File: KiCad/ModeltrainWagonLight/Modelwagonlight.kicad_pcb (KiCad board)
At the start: 2 copper layers, 19.3 x 10.2 mm, 13 parts, among them J1 Conn_01x02, J2 Conn_01x02, U1 NCP1117-ADJ_SOT223

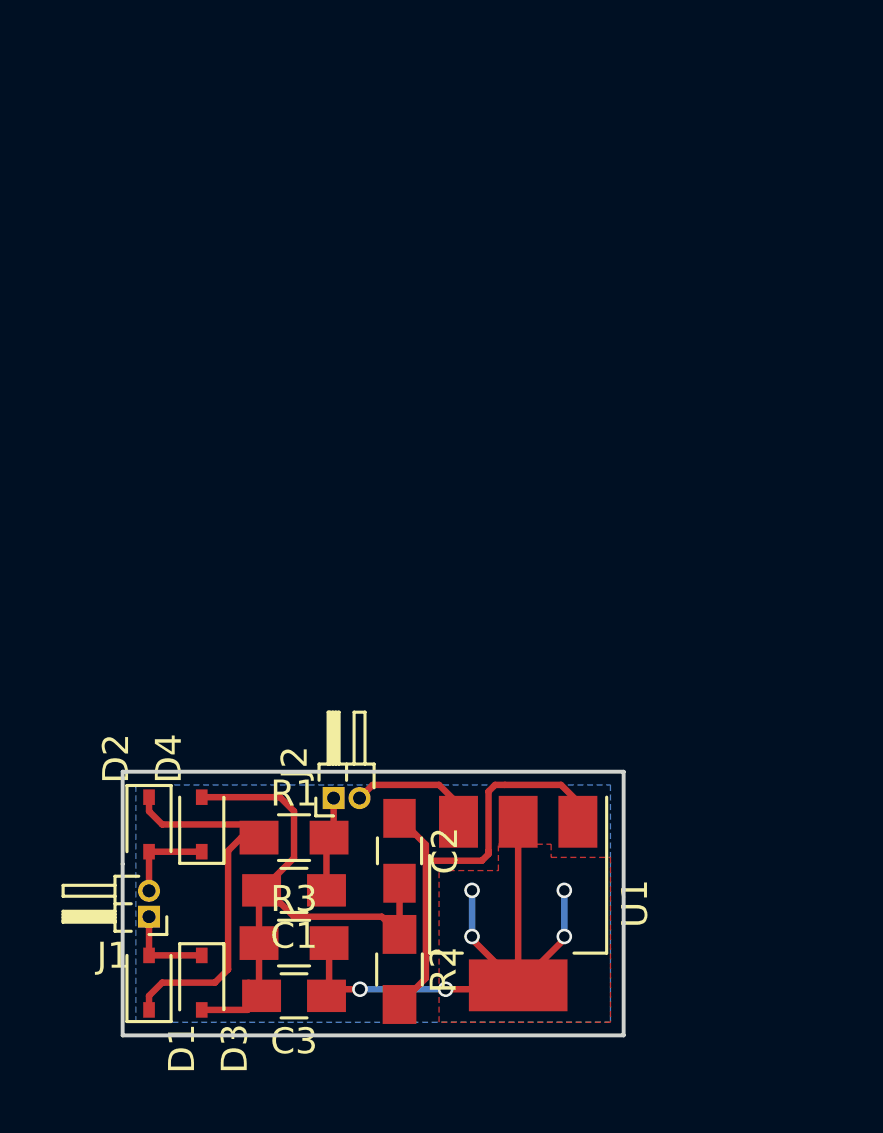
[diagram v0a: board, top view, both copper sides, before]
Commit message: Updated ModeltrainWagonLight/Modelwagonlight
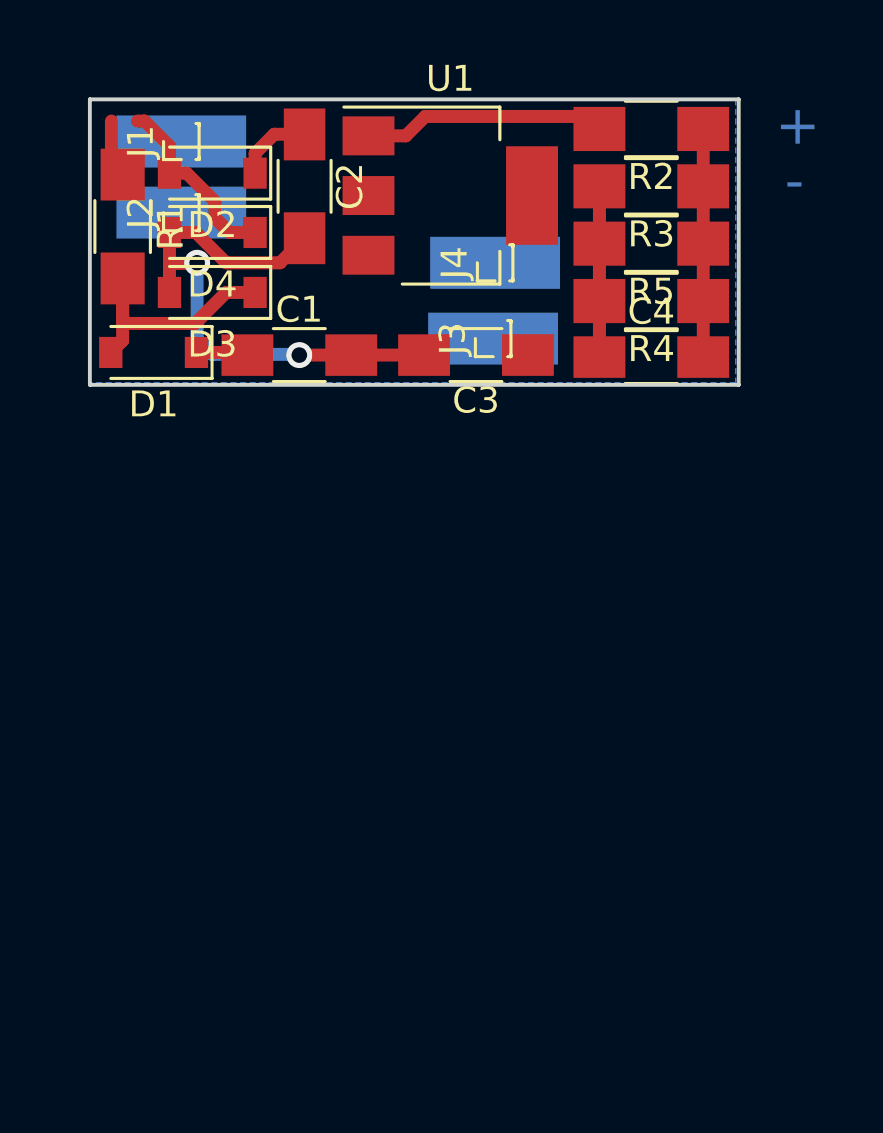
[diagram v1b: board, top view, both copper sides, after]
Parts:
- added C4: 10uF, Capacitors_SMD:C_1206_HandSoldering, F.Cu at (211.6, 120.9)
- added J3: Conn_01x01, Pin_Headers:Pin_Header_Straight_1x01_Pitch1.00mm, F.Cu at (205.5, 120.2)
- added J4: Conn_01x01, Pin_Headers:Pin_Header_Straight_1x01_Pitch1.00mm, F.Cu at (205.6, 117.3)
- added R4: 100R, Resistors_SMD:R_1206_HandSoldering, F.Cu at (211.6, 118.8)
- added R5: 100R, Resistors_SMD:R_1206_HandSoldering, F.Cu at (211.6, 116.6)
- C1: value 1uF -> 10uF; footprint Capacitors_SMD:C_0805_HandSoldering -> Capacitors_SMD:C_1206_HandSoldering
- C2: value 100nF -> 10uF; footprint Capacitors_SMD:C_0805_HandSoldering -> Capacitors_SMD:C_1206_HandSoldering
- C3: value 2.2uF -> 100nF; footprint Capacitors_SMD:C_0805_HandSoldering -> Capacitors_SMD:C_1206_HandSoldering
- D1, D2, D3, D4: value 1n4148 -> STPS0540Z; footprint Diodes_SMD:D_SOD-323 -> Diodes_SMD:D_SOD-123
- J1, J2: value Conn_01x02 -> Conn_01x01; footprint Pin_Headers:Pin_Header_Angled_1x02_Pitch1.00mm -> Pin_Headers:Pin_Header_Straight_1x01_Pitch1.00mm
- R1, R2, R3: footprint Resistors_SMD:R_0805_HandSoldering -> Resistors_SMD:R_1206_HandSoldering
- U1: value NCP1117-ADJ_SOT223 -> LT3082-SOT223-3_Fnl2295277
- moved R2 33.8 mm to (211.6, 112.1), turned to 180 degrees
- moved R3 32.2 mm to (211.6, 114.4), turned to 180 degrees
- moved J1 29.9 mm to (193.5, 112.6), turned to 90 degrees
- moved U1 27.4 mm to (203.9, 114.7), turned to 0 degrees
- moved D3 26.6 mm to (194.7, 118.4), turned to 180 degrees
- moved C2 25.9 mm to (198.3, 114.4)
- moved C3 25.7 mm to (204.9, 120.9)
- moved D2 25.2 mm to (194.7, 113.8), turned to 180 degrees
- moved R1 24.5 mm to (191.3, 115.9), turned to 270 degrees
- moved D1 24.3 mm to (192.5, 120.8), turned to 180 degrees
- moved J2 23.3 mm to (193.5, 115.4)
- moved D4 22.8 mm to (194.7, 116.1), turned to 180 degrees
- moved C1 20.6 mm to (198.1, 120.9), turned to 0 degrees
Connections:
- C2 pad 1: Net-(C2-Pad1) -> Net-(C1-Pad1)
- D1 pad 1: Net-(D1-Pad1) -> Net-(C1-Pad1)
- D2 pad 1: Net-(D1-Pad1) -> Net-(C1-Pad1)
- J1 pad 1: Net-(D1-Pad2) -> Net-(J1-Pad1)
- J2 pad 1: Net-(C1-Pad1) -> Net-(D2-Pad2)
- R1 pad 1: Net-(D1-Pad1) -> Net-(J1-Pad1)
- R1 pad 2: Net-(C1-Pad1) -> Net-(D1-Pad2)
- R2 pad 2: Net-(C2-Pad1) -> Net-(C3-Pad1)
- R3 pad 2: Net-(C3-Pad1) -> Net-(C4-Pad1)
- U1 pad 1: Net-(C2-Pad1) -> Net-(C3-Pad1)
- U1 pad 2: Net-(C3-Pad1) -> Net-(C4-Pad1)
- U1 pad 3: Net-(J2-Pad2) -> Net-(J4-Pad1)
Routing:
- net Net-(C2-Pad1): track 18.1 -> 0.00 mm
- net Net-(C3-Pad1): track 24.7 -> 9.41 mm, vias 6 -> 0
- net Net-(D1-Pad1): track 15.2 -> 0.00 mm
- net Net-(C1-Pad2): track 22.7 -> 30.2 mm, vias 0 -> 2
- net Net-(D1-Pad2): track 3.52 -> 10.4 mm
- net Net-(C4-Pad1): track 0.00 -> 6.60 mm
- net Net-(J2-Pad2): track 5.01 -> 0.00 mm
- net Net-(D2-Pad2): track 3.54 -> 7.30 mm
- net Net-(J1-Pad1): track 0.00 -> 2.24 mm
- net Net-(C1-Pad1): track 3.92 -> 5.13 mm
- added copper zone on B.Cu, net Net-(C4-Pad1)
- removed copper zone on B.Cu, net Net-(C3-Pad1)
- removed copper zone on F.Cu, net Net-(C3-Pad1)
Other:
- board size 19.3 x 10.2 mm -> 25 x 11 mm
- net class Default: trace_width 0.25 -> 0.5; via_dia 0.6 -> 1; via_drill 0.4 -> 0.6
- board text added: "+"
- board text added: "-"

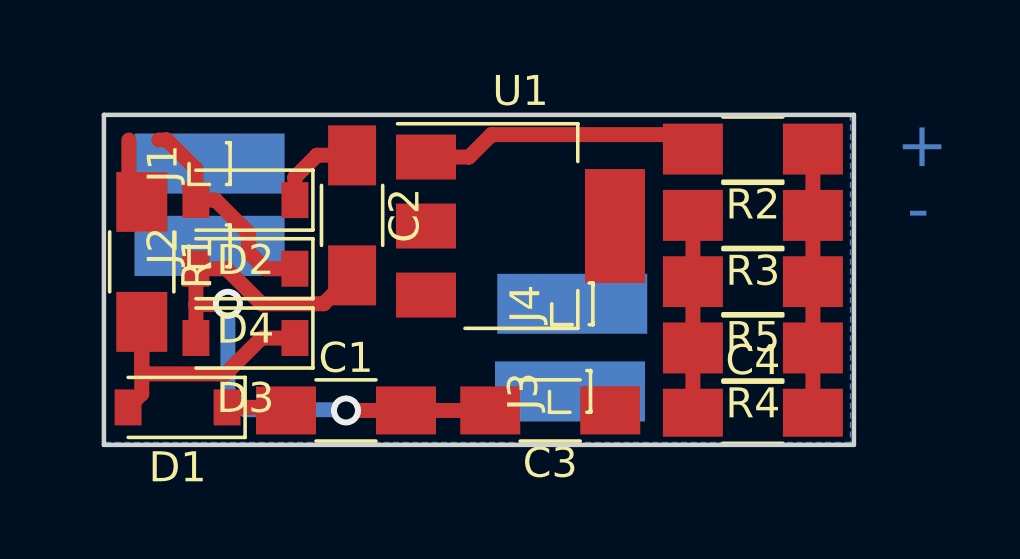
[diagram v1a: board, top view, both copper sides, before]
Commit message: Updated and finished for proto the ModeltrainWagonLight. Generated gerber files etc
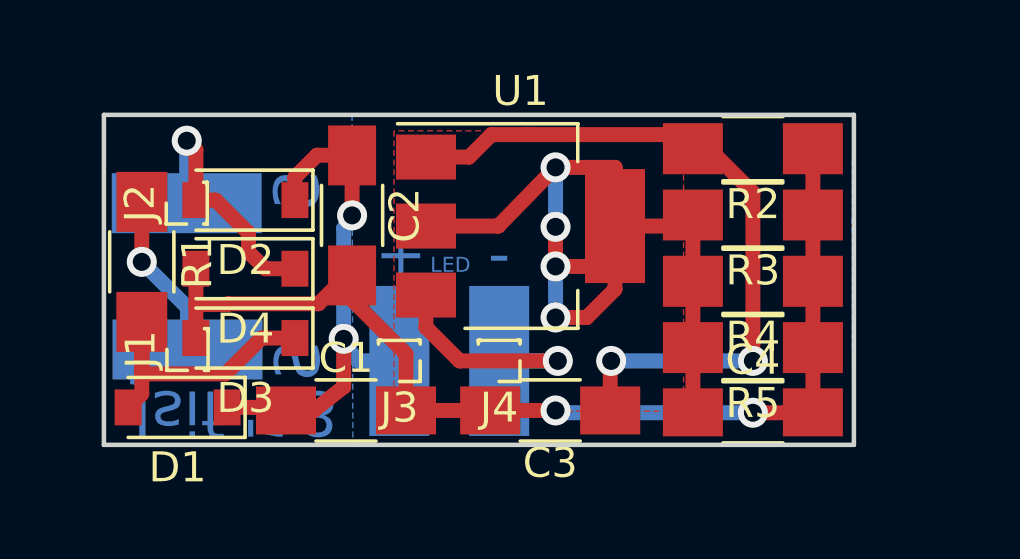
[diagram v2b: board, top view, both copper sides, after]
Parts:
- J1, J2, J3, J4: footprint Pin_Headers:Pin_Header_Straight_1x01_Pitch1.00mm -> Contact_fingers:Contact_Finger
- moved J1 6.24 mm to (192.8, 118.8)
- moved J3 5.78 mm to (199.8, 119.2), turned to 180 degrees
- moved J4 3.09 mm to (203.2, 119.2), turned to 180 degrees
- moved R4 2.22 mm to (211.6, 116.5)
- moved R5 2.20 mm to (211.6, 118.8)
- moved J2 1.61 mm to (192.8, 113.9)
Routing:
- net Net-(C4-Pad1): track 6.60 -> 30.9 mm, vias 0 -> 4
- net Net-(C3-Pad1): track 9.41 -> 24.0 mm, vias 0 -> 2
- net Net-(C1-Pad1): track 5.13 -> 17.4 mm, vias 0 -> 2
- net Net-(J4-Pad1): track 0.00 -> 7.89 mm, vias 0 -> 1
- net Net-(C1-Pad2): track 30.2 -> 35.6 mm
- net Net-(J1-Pad1): track 2.24 -> 6.16 mm, vias 0 -> 1
- net Net-(D2-Pad2): track 7.30 -> 8.81 mm, vias 0 -> 1
- added copper zone on F.Cu, net Net-(C4-Pad1)
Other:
- board text added: "Jsif '18"
- board text added: "LED"
- board text added: "S"
